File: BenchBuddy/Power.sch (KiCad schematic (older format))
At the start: 0 parts

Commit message: Week3 part 1
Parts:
- added C? (x2): C, ~, symbol C
- added F? (x4): FUSE, ~, symbol FUSE
- added L? (x2): INDUCTOR, ~, symbol INDUCTOR
- added P?: CONN_12X2, symbol CONN_12X2
- added R?: R, ~, symbol R
- added SW?: SWITCH_INV, ~, symbol SWITCH_INV
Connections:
- net labels added: +12P, +12V, +3,3V, +5V, -12P, -12V, GND
- wire segments 0 -> 36

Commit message: Week3 Part 2
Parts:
- removed F? (x4): FUSE, ~, symbol FUSE
- added TH? (x4): THERMISTOR, ~, symbol THERMISTOR
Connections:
- net labels added: +12C
- wire segments 36 -> 37
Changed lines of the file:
@@
 EESchema Schematic File Version 2
+LIBS:BenchBuddy
 LIBS:power
 LIBS:device
@@
 $Descr A4 11693 8268
 encoding utf-8
-Sheet 5 9
+Sheet 4 9
 Title ""
-Date "5 mar 2014"
+Date "7 mar 2014"
 Rev ""
 Comp ""
@@
 $EndComp
 $Comp
-L FUSE F?
-U 1 1 5316CC1F
-P 3300 2600
-F 0 "F?" H 3400 2650 40  0000 C CNN
-F 1 "FUSE" H 3200 2550 40  0000 C CNN
-F 2 "~" H 3300 2600 60  0000 C CNN
-F 3 "~" H 3300 2600 60  0000 C CNN
-	1    3300 2600
-	1    0    0    -1
-$EndComp
-$Comp
-L FUSE F?
-U 1 1 5316CC2E
-P 3800 2800
-F 0 "F?" H 3900 2850 40  0000 C CNN
-F 1 "FUSE" H 3700 2750 40  0000 C CNN
-F 2 "~" H 3800 2800 60  0000 C CNN
-F 3 "~" H 3800 2800 60  0000 C CNN
-	1    3800 2800
-	1    0    0    -1
-$EndComp
-$Comp
-L FUSE F?
-U 1 1 5316CC3D
-P 4300 3000
-F 0 "F?" H 4400 3050 40  0000 C CNN
-F 1 "FUSE" H 4200 2950 40  0000 C CNN
-F 2 "~" H 4300 3000 60  0000 C CNN
-F 3 "~" H 4300 3000 60  0000 C CNN
-	1    4300 3000
-	1    0    0    -1
-$EndComp
-$Comp
-L FUSE F?
-U 1 1 5316CC4C
-P 4800 3200
-F 0 "F?" H 4900 3250 40  0000 C CNN
-F 1 "FUSE" H 4700 3150 40  0000 C CNN
-F 2 "~" H 4800 3200 60  0000 C CNN
-F 3 "~" H 4800 3200 60  0000 C CNN
-	1    4800 3200
-	1    0    0    -1
-$EndComp
-$Comp
 L SWITCH_INV SW?
 U 1 1 5316CC5B
@@
 $EndComp
 Wire Wire Line
-	2700 2600 3050 2600
+	2700 2600 3300 2600
 Wire Wire Line
 	2700 2800 3550 2800
@@
 	8400 4350 8400 4500
 Connection ~ 7650 4350
+Wire Wire Line
+	2950 3000 2950 2250
+Connection ~ 2950 3000
+$Comp
+L +12C #PWR?
+U 1 1 5319216B
+P 2950 2250
+F 0 "#PWR?" H 2950 2220 30  0001 C CNN
+F 1 "+12C" H 2950 2360 40  0000 C CNN
+F 2 "~" H 2950 2250 60  0000 C CNN
+F 3 "~" H 2950 2250 60  0000 C CNN
+	1    2950 2250
+	1    0    0    -1
+$EndComp
+$Comp
+L THERMISTOR TH?
+U 1 1 531926F2
+P 4800 3200
+F 0 "TH?" V 4900 3250 50  0000 C CNN
+F 1 "THERMISTOR" V 4700 3200 50  0000 C CNN
+F 2 "~" H 4800 3200 60  0000 C CNN
+F 3 "~" H 4800 3200 60  0000 C CNN
+	1    4800 3200
+	0    -1   -1   0
+$EndComp
+$Comp
+L THERMISTOR TH?
+U 1 1 53192706
+P 4300 3000
+F 0 "TH?" V 4400 3050 50  0000 C CNN
+F 1 "THERMISTOR" V 4200 3000 50  0000 C CNN
+F 2 "~" H 4300 3000 60  0000 C CNN
+F 3 "~" H 4300 3000 60  0000 C CNN
+	1    4300 3000
+	0    -1   -1   0
+$EndComp
+$Comp
+L THERMISTOR TH?
+U 1 1 5319270C
+P 3800 2800
+F 0 "TH?" V 3900 2850 50  0000 C CNN
+F 1 "THERMISTOR" V 3700 2800 50  0000 C CNN
+F 2 "~" H 3800 2800 60  0000 C CNN
+F 3 "~" H 3800 2800 60  0000 C CNN
+	1    3800 2800
+	0    -1   -1   0
+$EndComp
+$Comp
+L THERMISTOR TH?
+U 1 1 53192712
+P 3300 2600
+F 0 "TH?" V 3400 2650 50  0000 C CNN
+F 1 "THERMISTOR" V 3200 2600 50  0000 C CNN
+F 2 "~" H 3300 2600 60  0000 C CNN
+F 3 "~" H 3300 2600 60  0000 C CNN
+	1    3300 2600
+	0    -1   -1   0
+$EndComp
 $EndSCHEMATC

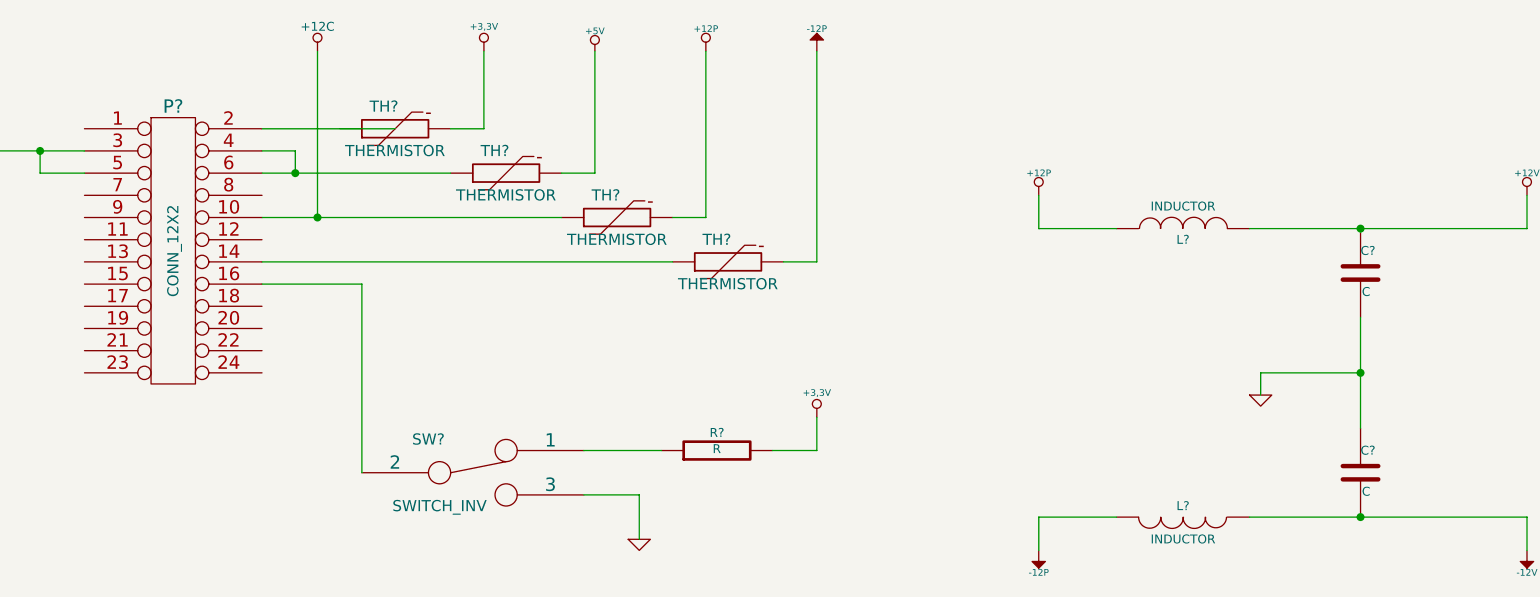
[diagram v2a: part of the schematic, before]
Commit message: Colocação dos Componentes Relé
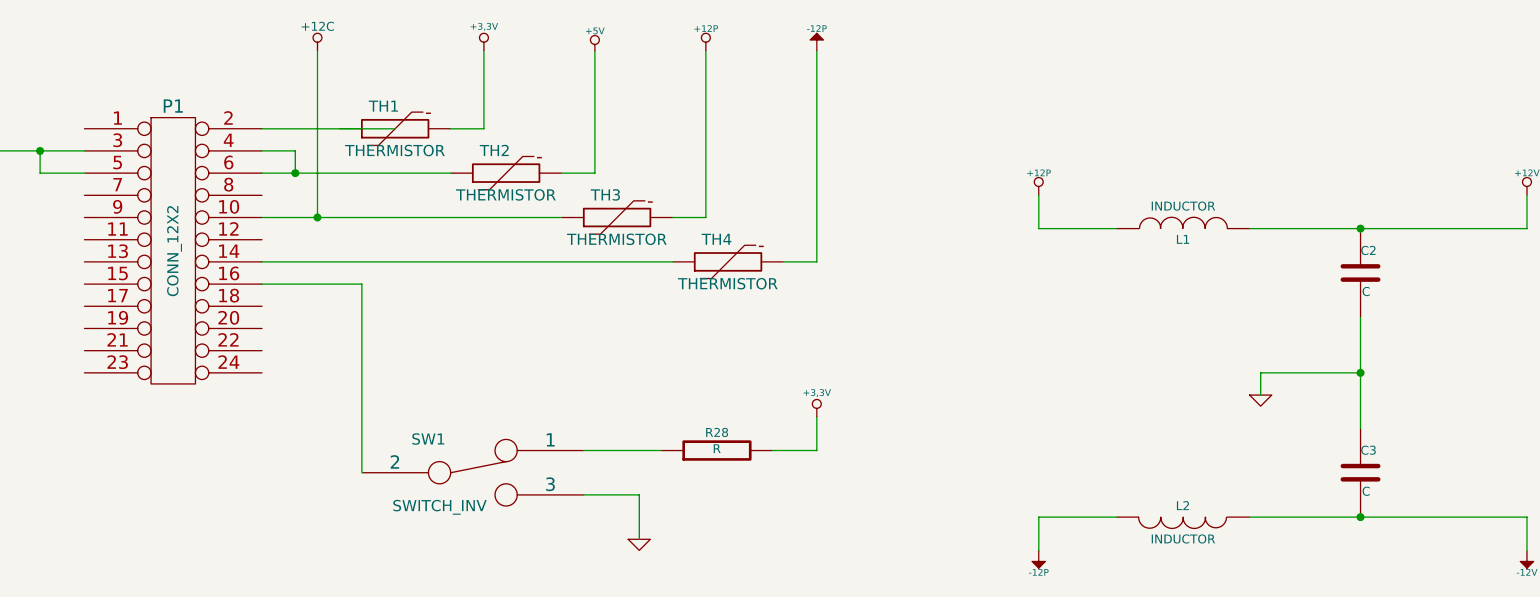
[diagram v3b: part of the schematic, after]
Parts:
- gave numbers to parts that had none: 11
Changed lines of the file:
@@
 Sheet 4 9
 Title ""
-Date "7 mar 2014"
+Date "9 mar 2014"
 Rev ""
 Comp ""
@@
 $EndDescr
 $Comp
-L CONN_12X2 P?
+L CONN_12X2 P1
 U 1 1 5316CB7F
 P 2300 3150
-F 0 "P?" H 2300 3800 60  0000 C CNN
+F 0 "P1" H 2300 3800 60  0000 C CNN
 F 1 "CONN_12X2" V 2300 3150 50  0000 C CNN
 F 2 "" H 2300 3150 60  0000 C CNN
@@
 $EndComp
 $Comp
-L +3,3V #PWR?
+L +3,3V #PWR15
 U 1 1 5316CB90
 P 3700 2250
-F 0 "#PWR?" H 3700 2210 30  0001 C CNN
+F 0 "#PWR15" H 3700 2210 30  0001 C CNN
 F 1 "+3,3V" H 3700 2360 30  0000 C CNN
 F 2 "" H 3700 2250 60  0000 C CNN
@@
 $EndComp
 $Comp
-L +5V #PWR?
+L +5V #PWR16
 U 1 1 5316CB9F
 P 4200 2250
-F 0 "#PWR?" H 4200 2340 20  0001 C CNN
+F 0 "#PWR16" H 4200 2340 20  0001 C CNN
 F 1 "+5V" H 4200 2340 30  0000 C CNN
 F 2 "" H 4200 2250 60  0000 C CNN
@@
 $EndComp
 $Comp
-L GND #PWR?
+L GND #PWR13
 U 1 1 5316CBAE
 P 1150 2850
-F 0 "#PWR?" H 1150 2850 30  0001 C CNN
+F 0 "#PWR13" H 1150 2850 30  0001 C CNN
 F 1 "GND" H 1150 2780 30  0001 C CNN
 F 2 "" H 1150 2850 60  0000 C CNN
@@
 $EndComp
 $Comp
-L SWITCH_INV SW?
+L SWITCH_INV SW1
 U 1 1 5316CC5B
 P 3650 4150
-F 0 "SW?" H 3450 4300 50  0000 C CNN
+F 0 "SW1" H 3450 4300 50  0000 C CNN
 F 1 "SWITCH_INV" H 3500 4000 50  0000 C CNN
 F 2 "~" H 3650 4150 60  0000 C CNN
@@
 	4200 2800 4200 2250
 $Comp
-L +12P #PWR?
+L +12P #PWR18
 U 1 1 5316CCD3
 P 4700 2250
-F 0 "#PWR?" H 4700 2220 30  0001 C CNN
+F 0 "#PWR18" H 4700 2220 30  0001 C CNN
 F 1 "+12P" H 4700 2350 30  0000 C CNN
 F 2 "" H 4700 2250 60  0000 C CNN
@@
 	4700 3000 4700 2250
 $Comp
-L -12P #PWR?
+L -12P #PWR19
 U 1 1 5316CE87
 P 5200 2250
-F 0 "#PWR?" H 5200 2380 20  0001 C CNN
+F 0 "#PWR19" H 5200 2380 20  0001 C CNN
 F 1 "-12P" H 5200 2350 30  0000 C CNN
 F 2 "" H 5200 2250 60  0000 C CNN
@@
 	3150 3300 3150 4150
 $Comp
-L GND #PWR?
+L GND #PWR17
 U 1 1 5316CF17
 P 4400 4450
-F 0 "#PWR?" H 4400 4450 30  0001 C CNN
+F 0 "#PWR17" H 4400 4450 30  0001 C CNN
 F 1 "GND" H 4400 4380 30  0001 C CNN
 F 2 "" H 4400 4450 60  0000 C CNN
@@
 	4400 4250 4400 4450
 $Comp
-L R R?
+L R R28
 U 1 1 5316CF36
 P 4750 4050
-F 0 "R?" V 4830 4050 40  0000 C CNN
+F 0 "R28" V 4830 4050 40  0000 C CNN
 F 1 "R" V 4757 4051 40  0000 C CNN
 F 2 "~" V 4680 4050 30  0000 C CNN
@@
 $EndComp
 $Comp
-L +3,3V #PWR?
+L +3,3V #PWR20
 U 1 1 5316CF4D
 P 5200 3900
-F 0 "#PWR?" H 5200 3860 30  0001 C CNN
+F 0 "#PWR20" H 5200 3860 30  0001 C CNN
 F 1 "+3,3V" H 5200 4010 30  0000 C CNN
 F 2 "" H 5200 3900 60  0000 C CNN
@@
 	5200 4050 5200 3900
 $Comp
-L INDUCTOR L?
+L INDUCTOR L1
 U 1 1 5316CFA4
 P 6850 3050
-F 0 "L?" V 6800 3050 40  0000 C CNN
+F 0 "L1" V 6800 3050 40  0000 C CNN
 F 1 "INDUCTOR" V 6950 3050 40  0000 C CNN
 F 2 "~" H 6850 3050 60  0000 C CNN
@@
 $EndComp
 $Comp
-L C C?
+L C C2
 U 1 1 5316CFB8
 P 7650 3250
-F 0 "C?" H 7650 3350 40  0000 L CNN
+F 0 "C2" H 7650 3350 40  0000 L CNN
 F 1 "C" H 7656 3165 40  0000 L CNN
 F 2 "~" H 7688 3100 30  0000 C CNN
@@
 $EndComp
 $Comp
-L C C?
+L C C3
 U 1 1 5316CFC5
 P 7650 4150
-F 0 "C?" H 7650 4250 40  0000 L CNN
+F 0 "C3" H 7650 4250 40  0000 L CNN
 F 1 "C" H 7656 4065 40  0000 L CNN
 F 2 "~" H 7688 4000 30  0000 C CNN
@@
 $EndComp
 $Comp
-L INDUCTOR L?
+L INDUCTOR L2
 U 1 1 5316CFCB
 P 6850 4350
-F 0 "L?" V 6800 4350 40  0000 C CNN
+F 0 "L2" V 6800 4350 40  0000 C CNN
 F 1 "INDUCTOR" V 6950 4350 40  0000 C CNN
 F 2 "~" H 6850 4350 60  0000 C CNN
@@
 	7150 4350 8400 4350
 $Comp
-L -12P #PWR?
+L -12P #PWR22
 U 1 1 5316D078
 P 6200 4500
-F 0 "#PWR?" H 6200 4630 20  0001 C CNN
+F 0 "#PWR22" H 6200 4630 20  0001 C CNN
 F 1 "-12P" H 6200 4600 30  0000 C CNN
 F 2 "" H 6200 4500 60  0000 C CNN
@@
 $EndComp
 $Comp
-L +12P #PWR?
+L +12P #PWR21
 U 1 1 5316D07E
 P 6200 2900
-F 0 "#PWR?" H 6200 2870 30  0001 C CNN
+F 0 "#PWR21" H 6200 2870 30  0001 C CNN
 F 1 "+12P" H 6200 3000 30  0000 C CNN
 F 2 "" H 6200 2900 60  0000 C CNN
@@
 	6200 4350 6200 4500
 $Comp
-L GND #PWR?
+L GND #PWR23
 U 1 1 5316D0C4
 P 7200 3800
-F 0 "#PWR?" H 7200 3800 30  0001 C CNN
+F 0 "#PWR23" H 7200 3800 30  0001 C CNN
 F 1 "GND" H 7200 3730 30  0001 C CNN
 F 2 "" H 7200 3800 60  0000 C CNN
@@
 Connection ~ 7650 3700
 $Comp
-L +12V #PWR?
+L +12V #PWR24
 U 1 1 5316D0EF
 P 8400 2900
-F 0 "#PWR?" H 8400 2850 20  0001 C CNN
+F 0 "#PWR24" H 8400 2850 20  0001 C CNN
 F 1 "+12V" H 8400 3000 30  0000 C CNN
 F 2 "" H 8400 2900 60  0000 C CNN
@@
 $EndComp
 $Comp
-L -12V #PWR?
+L -12V #PWR25
 U 1 1 5316D0FE
 P 8400 4500
-F 0 "#PWR?" H 8400 4630 20  0001 C CNN
+F 0 "#PWR25" H 8400 4630 20  0001 C CNN
 F 1 "-12V" H 8400 4600 30  0000 C CNN
 F 2 "" H 8400 4500 60  0000 C CNN
@@
 Connection ~ 2950 3000
 $Comp
-L +12C #PWR?
+L +12C #PWR14
 U 1 1 5319216B
 P 2950 2250
-F 0 "#PWR?" H 2950 2220 30  0001 C CNN
+F 0 "#PWR14" H 2950 2220 30  0001 C CNN
 F 1 "+12C" H 2950 2360 40  0000 C CNN
 F 2 "~" H 2950 2250 60  0000 C CNN
@@
 $EndComp
 $Comp
-L THERMISTOR TH?
+L THERMISTOR TH4
 U 1 1 531926F2
 P 4800 3200
-F 0 "TH?" V 4900 3250 50  0000 C CNN
+F 0 "TH4" V 4900 3250 50  0000 C CNN
 F 1 "THERMISTOR" V 4700 3200 50  0000 C CNN
 F 2 "~" H 4800 3200 60  0000 C CNN
@@
 $EndComp
 $Comp
-L THERMISTOR TH?
+L THERMISTOR TH3
 U 1 1 53192706
 P 4300 3000
-F 0 "TH?" V 4400 3050 50  0000 C CNN
+F 0 "TH3" V 4400 3050 50  0000 C CNN
 F 1 "THERMISTOR" V 4200 3000 50  0000 C CNN
 F 2 "~" H 4300 3000 60  0000 C CNN
@@
 $EndComp
 $Comp
-L THERMISTOR TH?
+L THERMISTOR TH2
 U 1 1 5319270C
 P 3800 2800
-F 0 "TH?" V 3900 2850 50  0000 C CNN
+F 0 "TH2" V 3900 2850 50  0000 C CNN
 F 1 "THERMISTOR" V 3700 2800 50  0000 C CNN
 F 2 "~" H 3800 2800 60  0000 C CNN
@@
 $EndComp
 $Comp
-L THERMISTOR TH?
+L THERMISTOR TH1
 U 1 1 53192712
 P 3300 2600
-F 0 "TH?" V 3400 2650 50  0000 C CNN
+F 0 "TH1" V 3400 2650 50  0000 C CNN
 F 1 "THERMISTOR" V 3200 2600 50  0000 C CNN
 F 2 "~" H 3300 2600 60  0000 C CNN

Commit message: Pre layout
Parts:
- removed L2: INDUCTOR, ~, symbol INDUCTOR
- added C13: C, ~, symbol C
- added JP1, JP2, JP3, JP4: JUMPER, ~, symbol JUMPER
- added L1, L4: CM322522-220KL, ~, symbol INDUCTOR
- added TP1: CONN_1, symbol CONN_1
- L2: renamed from L1; value INDUCTOR -> CM322522-220KL; MFG Name (none) -> BOURNS INC; MFG Part Number (none) -> CM322522-220KL
- P1: value CONN_12X2 -> 24 Pin MiniFit JR; MFG Name (none) -> Molex; MFG Part Number (none) -> 0039301240
- SW1: value SWITCH_INV -> Power Switch; MFG Name (none) -> C&K COMPONENTS; MFG Part Number (none) -> OS102011MA1QN1
- TH1, TH2, TH3, TH4: value THERMISTOR -> MINISMDC050F-2; MFG Name (none) -> TE CONNECTIVITY; MFG Part Number (none) -> MINISMDC050F-2
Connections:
- net +5V: now also C13.1, L1.2; no longer TH2.2
- net -12P: now also L4.2
- net -12V: now also L4.1
- net GND: now also C13.2, JP1.1, JP2.1, JP3.1, JP4.1, TP1.1
- net at P1.12 (P12): now also P1.2 (P2), TH1.1
- new net +5P: L1.1, TH2.2
- new net AGND: JP1.2
- new net GND_LED: JP3.2
- new net GND_PWR: JP2.2
- new net GND_RELAY: JP4.2
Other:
- note added: "Star Point"

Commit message: Pre layout 2
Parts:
- C13, C2, C3: value C -> 10u
- R28: value R -> 0
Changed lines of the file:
@@
 Sheet 2 9
 Title ""
-Date "30 mar 2014"
+Date "23 apr 2014"
 Rev ""
 Comp ""
@@
 P 4750 4050
 F 0 "R28" V 4830 4050 40  0000 C CNN
-F 1 "R" V 4757 4051 40  0000 C CNN
+F 1 "0" V 4757 4051 40  0000 C CNN
 F 2 "~" V 4680 4050 30  0000 C CNN
 F 3 "~" H 4750 4050 30  0000 C CNN
@@
 P 7650 3250
 F 0 "C2" H 7650 3350 40  0000 L CNN
-F 1 "C" H 7656 3165 40  0000 L CNN
+F 1 "10u" H 7656 3165 40  0000 L CNN
 F 2 "~" H 7688 3100 30  0000 C CNN
 F 3 "~" H 7650 3250 60  0000 C CNN
@@
 P 7650 4150
 F 0 "C3" H 7650 4250 40  0000 L CNN
-F 1 "C" H 7656 4065 40  0000 L CNN
+F 1 "10u" H 7656 4065 40  0000 L CNN
 F 2 "~" H 7688 4000 30  0000 C CNN
 F 3 "~" H 7650 4150 60  0000 C CNN
@@
 P 7650 2000
 F 0 "C13" H 7650 2100 40  0000 L CNN
-F 1 "C" H 7656 1915 40  0000 L CNN
+F 1 "10u" H 7656 1915 40  0000 L CNN
 F 2 "~" H 7688 1850 30  0000 C CNN
 F 3 "~" H 7650 2000 60  0000 C CNN
